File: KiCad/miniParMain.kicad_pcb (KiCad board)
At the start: 4 copper layers, 25 x 40 mm, 27 parts, among them J2 USB_C_Receptacle, J4 Conn_01x02_Pin, J5 secondBoard, SW2 SW_Push, U1 AS7341-DLGT, U2 IP4234CZ6, U5 AP7312-1833W6-7, U8 ESP8685, Y2 40MHz

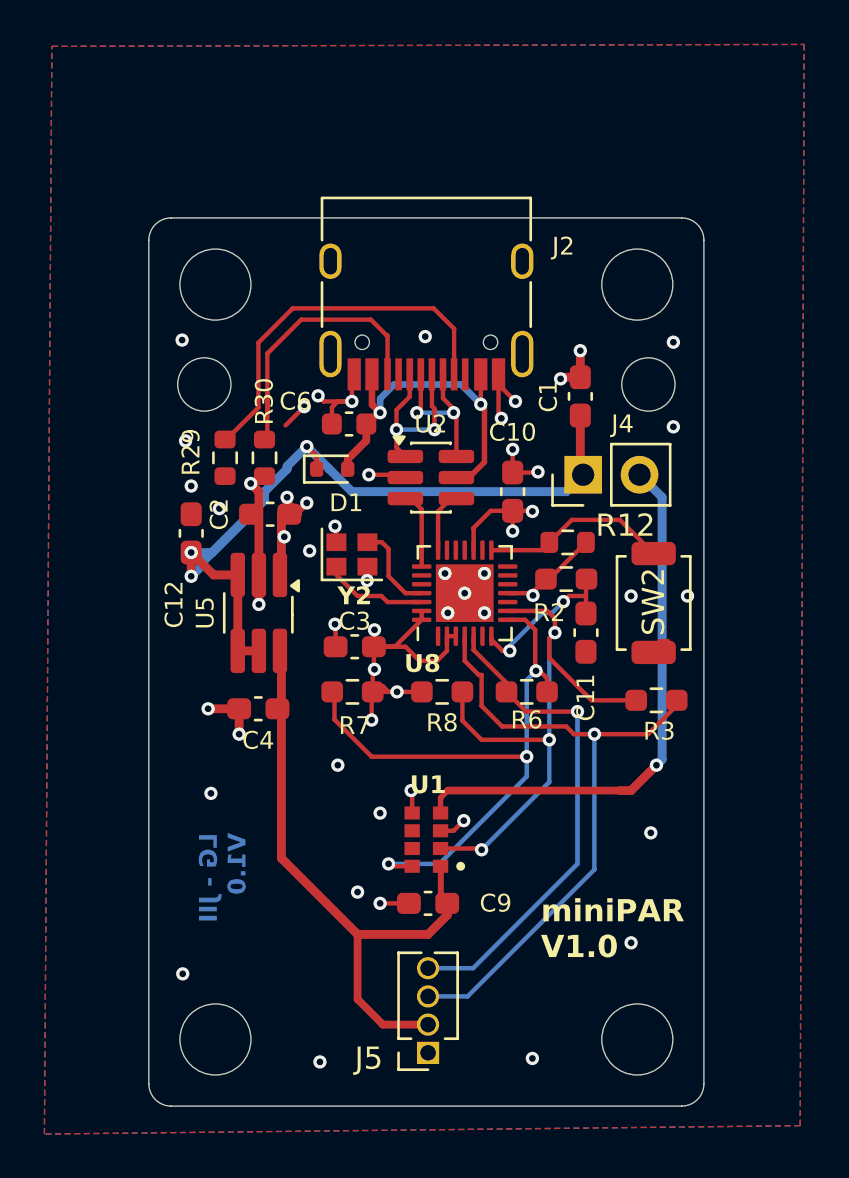
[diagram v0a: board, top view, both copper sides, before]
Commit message: PCB revision -> V 1.1
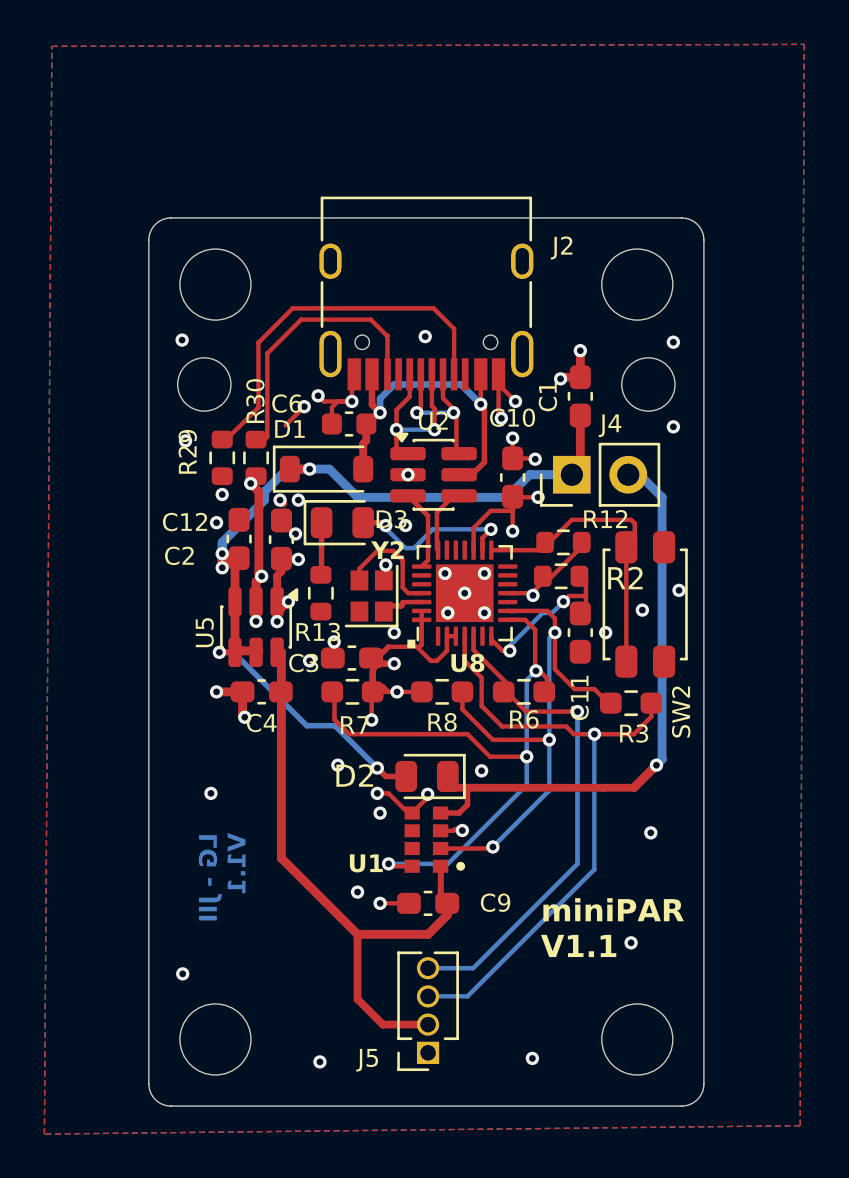
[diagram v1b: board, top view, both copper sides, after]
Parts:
- added D2: LED, Diode_SMD:D_0805_2012Metric, F.Cu at (100.0, 97.2)
- added D3: LED, Diode_SMD:D_0805_2012Metric, F.Cu at (96.2, 85.7)
- added R13: 5.1K, Resistor_SMD:R_0603_1608Metric, F.Cu at (95.2, 88.9)
- D1: footprint Diode_SMD:D_SOD-523 -> Diode_SMD:D_SOD-123
- R2: footprint Resistor_SMD:R_0603_1608Metric_Pad0.98x0.95mm_HandSolder -> Resistor_SMD:R_0603_1608Metric
- SW2: footprint Button_Switch_SMD:SW_SPST_TS-1088-xR025 -> Button_Switch_SMD:SW_SPST_EVQP2_ShortPushTravel_H2.1mm
- U5: footprint Package_TO_SOT_SMD:TSOT-23-6_HandSoldering -> Package_TO_SOT_SMD:TSOT-23-6
- moved C12 2.17 mm to (91.6, 86.5)
- moved Y2 2.07 mm to (97.5, 89.0), turned to 90 degrees
- moved C2 1.25 mm to (93.5, 86.5), turned to 90 degrees
- moved R3 1.15 mm to (109.2, 93.9)
- moved C4 0.78 mm to (92.6, 93.3)
- moved U5 0.65 mm to (92.3, 90.4)
- moved C10 0.64 mm to (103.9, 83.7)
- moved C3 0.52 mm to (96.6, 91.8)
- moved J4 0.51 mm to (106.6, 83.6)
- moved SW2 0.39 mm to (109.9, 89.4), turned to 90 degrees
- moved R30 0.38 mm to (92.3, 82.8)
- moved R2 0.26 mm to (106.1, 88.1)
- moved C11 0.25 mm to (106.9, 90.7)
- moved D1 0.25 mm to (95.5, 83.3)
- moved R12 0.19 mm to (106.2, 86.6)
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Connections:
- U8 pad 16: unconnected-(U8-GPIO10-Pad16) -> Net-(D3-A)
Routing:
- net Net-(D3-A): track 0.00 -> 7.75 mm, vias 0 -> 2
- net V+: track 36.3 -> 41.7 mm, vias 3 -> 5
- net BOOT: track 8.50 -> 13.2 mm
- net Net-(U8-XTAL_P): track 4.35 -> 1.84 mm
- net Net-(D3-K): track 0.00 -> 2.45 mm
- net V+3V: track 29.7 -> 28.0 mm, vias 10 -> 9
- net D+: track 3.42 -> 4.95 mm
- net GND: track 29.5 -> 28.0 mm, vias 44 -> 52
- net LED1ACT: track 24.8 -> 26.2 mm
- net SCL: track 27.7 -> 26.4 mm
- net SDA_2: track 29.6 -> 28.5 mm
- net Net-(U8-XTAL_N): track 4.12 -> 4.92 mm
- net CC2: track 12.8 -> 12.0 mm
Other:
- board text added: "."
- board text added: "LG - JII V1.1"
- board text added: "miniPAR V1.1"
- board text removed: "LG - JII V1.0"
- board text removed: "miniPAR V1.0"
